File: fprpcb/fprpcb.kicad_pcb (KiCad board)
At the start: 2 copper layers, 119.8 x 90.3 mm, 46 parts, among them J1 Conn_02x04_Odd_Even, J2 Conn_01x02, J3 Conn_01x03, J4 Conn_01x03, J5 Conn_01x03, J6 Conn_01x03, J7 Conn_01x06, J8 Conn_01x04, SW1 Conn_01x02_Pin, SW2 Conn_01x02_Pin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

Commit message: verifying all traces to be correct size and clearance
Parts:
- moved R4 1.10 mm to (119.1, 72.5)
- moved R10 1.10 mm to (155.9, 72.5)
- moved R6 1.10 mm to (143.6, 72.5)
- moved R8 1.10 mm to (131.3, 72.5)
- moved R13 0.97 mm to (168.6, 72.5)
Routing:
- net Net-(SW3-Pin_2): track 6.40 -> 15.2 mm
- net GND: track 502.1 -> 494.1 mm, vias 3 -> 4
- net Net-(SW4-Pin_2): track 6.60 -> 13.3 mm
- net Net-(SW2-Pin_2): track 6.60 -> 13.0 mm
- net /SW3: track 159.2 -> 164.6 mm
- net +3V3: track 55.2 -> 57.7 mm
- net /SW1: track 100.1 -> 101.4 mm
- net Net-(SW1-Pin_2): track 6.79 -> 5.60 mm
- net VDDA: track 117.8 -> 118.9 mm
- net Net-(SW5-Pin_2): track 6.23 -> 5.27 mm

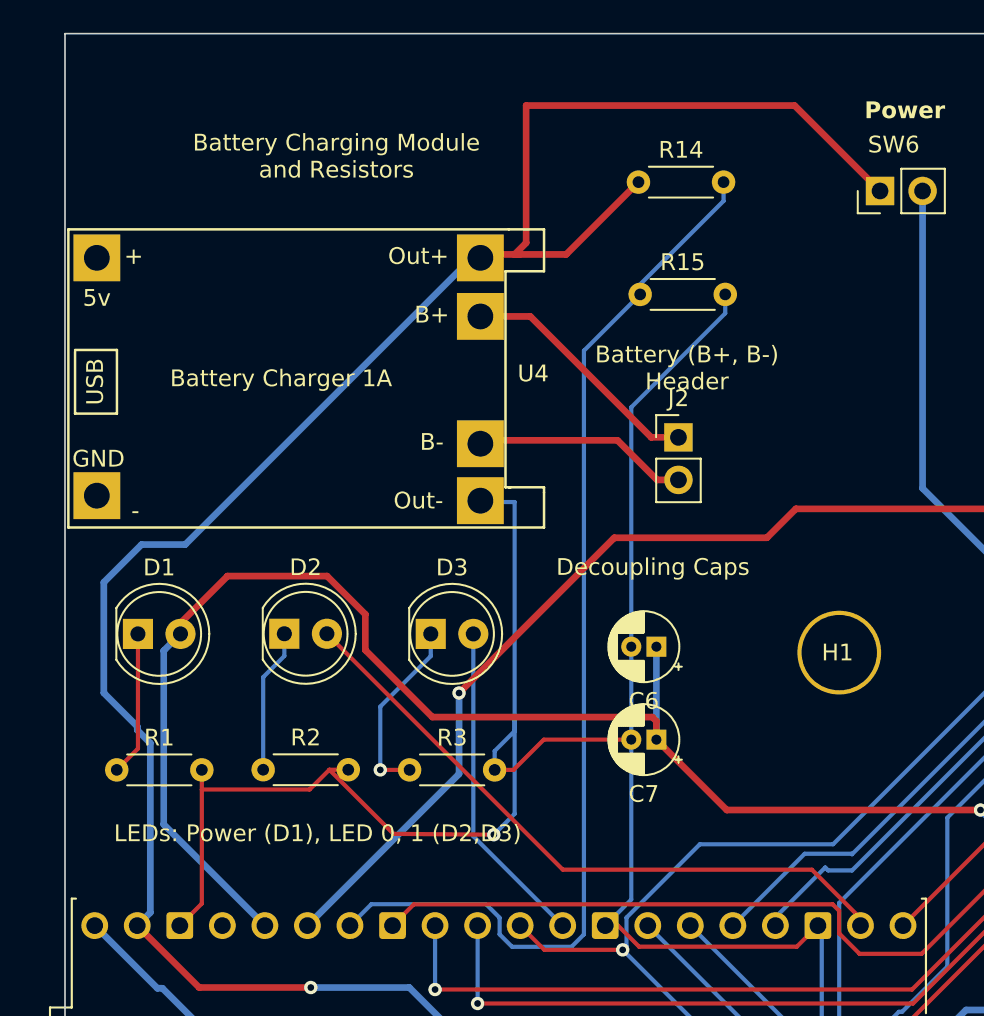
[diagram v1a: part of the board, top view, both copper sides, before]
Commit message: Updated FPRPCB based on 3/30 feedback
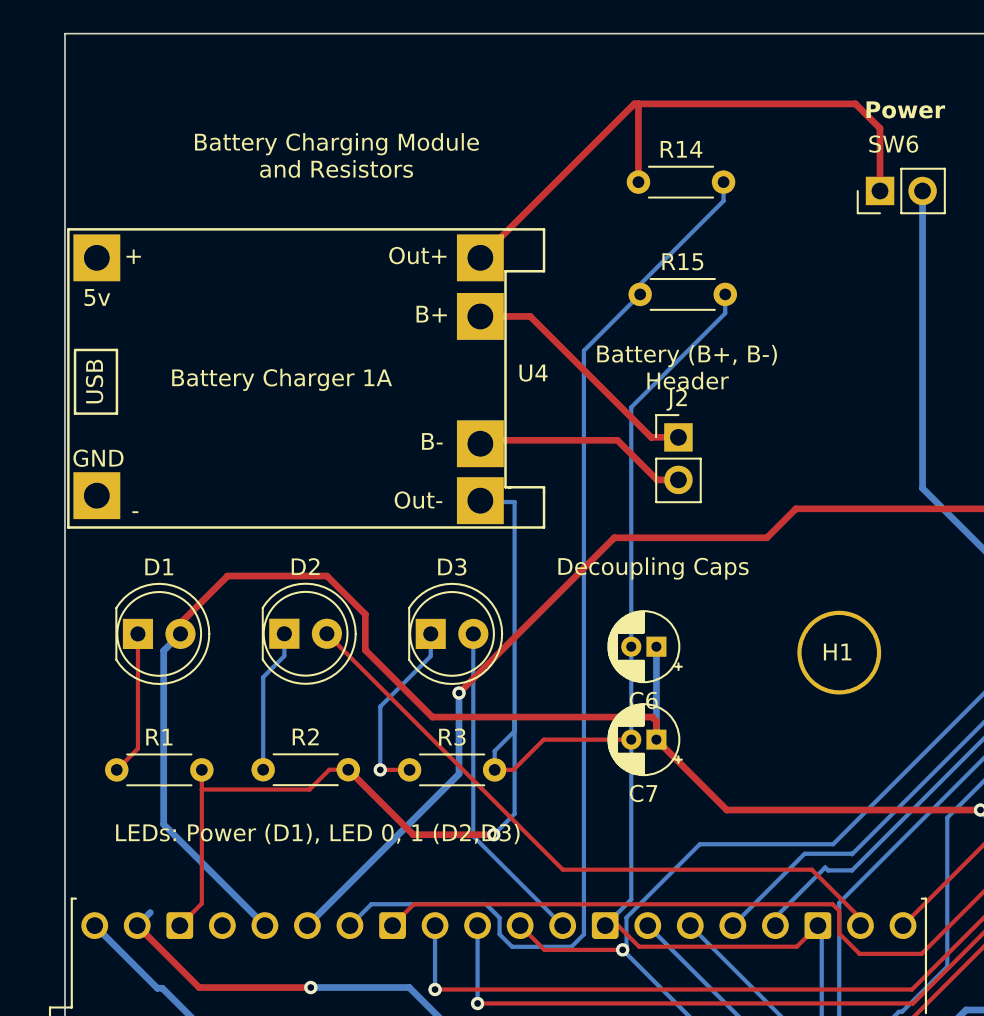
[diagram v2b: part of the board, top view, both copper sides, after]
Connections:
- R14 pad 1: VSYS -> Out+
- SW6 pad 1: VSYS -> Out+
- U4 pad 1: VSYS -> Out+
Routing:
- net VSYS: track 317.7 -> 222.4 mm
- net Out+: track 0.00 -> 36.7 mm
- net GND: track 494.1 -> 493.0 mm
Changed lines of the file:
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@@
   (net 49 "/B-")
   (net 50 "VSYS")
+  (net 51 "Out+")
   (footprint "LED_THT:LED_D5.0mm" (layer "F.Cu")
     (at 64.299 95.1484)
@@
       (stroke (width 0.15) (type solid)) (layer "F.SilkS"))
     (pad "1" thru_hole rect (at 24.6 1.7) (size 2.8 2.8) (drill 1.54) (layers "*.Cu" "*.Mask")
-      (net 50 "VSYS") (pinfunction "OUT+") (pintype "power_in"))
+      (net 51 "Out+") (pinfunction "OUT+") (pintype "power_in"))
     (pad "2" thru_hole rect (at 24.6 5.2) (size 2.8 2.8) (drill 1.54) (layers "*.Cu" "*.Mask")
       (net 48 "/B+") (pinfunction "B+") (pintype "power_in"))
@@
       (stroke (width 0.1) (type solid)) (layer "F.Fab"))
     (pad "1" thru_hole circle (at 0 0) (size 1.4 1.4) (drill 0.7) (layers "*.Cu" "*.Mask")
-      (net 50 "VSYS") (pintype "passive"))
+      (net 51 "Out+") (pintype "passive"))
     (pad "2" thru_hole oval (at 5.08 0) (size 1.4 1.4) (drill 0.7) (layers "*.Cu" "*.Mask")
       (net 45 "/GP28_ADC2") (pintype "passive"))
@@
       (stroke (width 0.1) (type solid)) (layer "F.Fab"))
     (pad "1" thru_hole rect (at 0 0 90) (size 1.7 1.7) (drill 1) (layers "*.Cu" "*.Mask")
-      (net 50 "VSYS") (pinfunction "Pin_1") (pintype "passive"))
+      (net 51 "Out+") (pinfunction "Pin_1") (pintype "passive"))
     (pad "2" thru_hole oval (at 0 2.54 90) (size 1.7 1.7) (drill 1) (layers "*.Cu" "*.Mask")
       (net 50 "VSYS") (pinfunction "Pin_2") (pintype "passive"))
@@
   (segment (start 148.0092 82.4039) (end 158.556 82.4039) (width 0.25) (layer "F.Cu") (net 2))
   (segment (start 68.114 104.439) (end 68.114 103.2674) (width 0.25) (layer "F.Cu") (net 2))
-  (segment (start 75.7291 103.2584) (end 79.5571 107.0864) (width 0.25) (layer "F.Cu") (net 2))
   (segment (start 89.154 138.7856) (end 76.2508 138.7856) (width 0.25) (layer "F.Cu") (net 2))
+  (segment (start 76.856 103.2584) (end 80.7348 107.1372) (width 0.4) (layer "F.Cu") (net 2))
   (segment (start 148.0092 82.4039) (end 146.9129 83.5002) (width 0.25) (layer "F.Cu") (net 2))
   (segment (start 103.6707 131.5712) (end 104.898 130.3439) (width 0.25) (layer "F.Cu") (net 2))
+  (segment (start 80.7348 107.1372) (end 85.5472 107.1372) (width 0.4) (layer "F.Cu") (net 2))
   (segment (start 88.5319 101.4604) (end 86.7249 103.2674) (width 0.25) (layer "F.Cu") (net 2))
   (segment (start 66.798 130.3439) (end 67.0649 130.3439) (width 0.25) (layer "F.Cu") (net 2))
@@
   (segment (start 68.114 111.2479) (end 68.114 104.439) (width 0.25) (layer "F.Cu") (net 2))
   (segment (start 124.51 85.4456) (end 135.5811 85.4456) (width 0.25) (layer "F.Cu") (net 2))
-  (segment (start 79.5571 107.0864) (end 85.5472 107.1372) (width 0.25) (layer "F.Cu") (net 2))
   (segment (start 146.9129 83.828) (end 146.2138 84.5271) (width 0.25) (layer "F.Cu") (net 2))
   (segment (start 162.3463 71.1708) (end 172.5676 71.1708) (width 0.4) (layer "F.Cu") (net 2))
@@
   (segment (start 65.8368 106.5227) (end 71.878 112.5639) (width 0.4) (layer "B.Cu") (net 6))
   (segment (start 95.2538 101.4604) (end 95.2538 95.9104) (width 0.4) (layer "B.Cu") (net 6))
-  (segment (start 63.034 103.2674) (end 64.299 102.0024) (width 0.25) (layer "F.Cu") (net 7))
   (segment (start 64.299 102.0024) (end 64.299 95.1484) (width 0.25) (layer "F.Cu") (net 7))
+  (segment (start 64.299 102.0024) (end 63.034 103.2674) (width 0.25) (layer "F.Cu") (net 7))
   (segment (start 71.776 97.7313) (end 73.041 96.4663) (width 0.25) (layer "B.Cu") (net 8))
   (segment (start 73.041 95.1394) (end 73.041 96.4663) (width 0.25) (layer "B.Cu") (net 8))
@@
   (segment (start 95.2939 85.9536) (end 92.9314 83.5911) (width 0.4) (layer "F.Cu") (net 49))
   (segment (start 92.9314 83.5911) (end 84.7749 83.5911) (width 0.4) (layer "F.Cu") (net 49))
-  (segment (start 87.4776 71.8026) (end 86.7891 72.4911) (width 0.4) (layer "F.Cu") (net 50))
   (segment (start 120.0404 95.3516) (end 120.0404 101.0412) (width 0.4) (layer "F.Cu") (net 50))
-  (segment (start 84.7749 72.4911) (end 84.5712 72.6948) (width 0.4) (layer "F.Cu") (net 50))
-  (segment (start 87.0712 72.4911) (end 84.7749 72.4911) (width 0.4) (layer "F.Cu") (net 50))
   (segment (start 96.4692 125.4252) (end 98.298 127.254) (width 0.4) (layer "F.Cu") (net 50))
   (segment (start 78.8416 143.8148) (end 82.042 147.0152) (width 0.4) (layer "F.Cu") (net 50))
-  (segment (start 87.4776 63.6016) (end 87.4776 71.8026) (width 0.4) (layer "F.Cu") (net 50))
-  (segment (start 103.504 63.6016) (end 87.4776 63.6016) (width 0.4) (layer "F.Cu") (net 50))
   (segment (start 118.0592 143.5608) (end 118.0592 142.2908) (width 0.4) (layer "F.Cu") (net 50))
   (segment (start 82.042 147.0152) (end 114.6048 147.0152) (width 0.4) (layer "F.Cu") (net 50))
   (segment (start 67.9551 116.261) (end 74.6204 116.261) (width 0.4) (layer "F.Cu") (net 50))
-  (segment (start 89.8657 72.4911) (end 94.1832 68.1736) (width 0.4) (layer "F.Cu") (net 50))
   (segment (start 117.856 127.254) (end 117.9068 127.2032) (width 0.4) (layer "F.Cu") (net 50))
   (segment (start 116.2304 145.3896) (end 118.0592 143.5608) (width 0.4) (layer "F.Cu") (net 50))
@@
   (segment (start 116.2304 91.5416) (end 120.0404 95.3516) (width 0.4) (layer "F.Cu") (net 50))
   (segment (start 116.2304 145.5928) (end 116.2304 145.3896) (width 0.4) (layer "F.Cu") (net 50))
-  (segment (start 108.6054 68.703) (end 103.504 63.6016) (width 0.4) (layer "F.Cu") (net 50))
-  (segment (start 86.7891 72.4911) (end 87.0712 72.4911) (width 0.4) (layer "F.Cu") (net 50))
   (segment (start 98.298 127.254) (end 117.856 127.254) (width 0.4) (layer "F.Cu") (net 50))
-  (segment (start 87.0712 72.4911) (end 89.8657 72.4911) (width 0.4) (layer "F.Cu") (net 50))
   (segment (start 64.258 112.5639) (end 67.9551 116.261) (width 0.4) (layer "F.Cu") (net 50))
   (segment (start 114.6048 147.0152) (end 116.0272 145.5928) (width 0.4) (layer "F.Cu") (net 50))
@@
   (via (at 116.2304 145.5928) (size 0.8) (drill 0.4) (layers "F.Cu" "B.Cu") (net 50))
   (segment (start 120.0404 101.0412) (end 121.9708 101.0412) (width 0.4) (layer "B.Cu") (net 50))
-  (segment (start 67.1197 89.8144) (end 64.516 89.8144) (width 0.4) (layer "B.Cu") (net 50))
   (segment (start 127 144.0688) (end 127 114.5032) (width 0.4) (layer "B.Cu") (net 50))
   (segment (start 111.1454 68.703) (end 111.1454 86.4566) (width 0.4) (layer "B.Cu") (net 50))
   (segment (start 125.476 145.5928) (end 127 144.0688) (width 0.4) (layer "B.Cu") (net 50))
-  (segment (start 65.0368 101.6676) (end 65.0368 111.7851) (width 0.4) (layer "B.Cu") (net 50))
   (segment (start 80.4994 116.261) (end 74.6204 116.261) (width 0.4) (layer "B.Cu") (net 50))
   (segment (start 127 114.5032) (end 131.3942 110.109) (width 0.4) (layer "B.Cu") (net 50))
@@
   (segment (start 122.3264 101.0412) (end 122.2248 101.0412) (width 0.4) (layer "B.Cu") (net 50))
   (segment (start 118.0592 127.3556) (end 118.0592 142.2908) (width 0.4) (layer "B.Cu") (net 50))
-  (segment (start 64.258 100.6673) (end 64.258 100.8888) (width 0.4) (layer "B.Cu") (net 50))
   (segment (start 122.2248 101.0412) (end 120.0404 101.0412) (width 0.4) (layer "B.Cu") (net 50))
   (segment (start 89.6636 125.4252) (end 80.4994 116.261) (width 0.4) (layer "B.Cu") (net 50))
   (segment (start 122.2248 101.0412) (end 121.9708 101.0412) (width 0.4) (layer "B.Cu") (net 50))
-  (segment (start 84.443 72.4911) (end 67.1197 89.8144) (width 0.4) (layer "B.Cu") (net 50))
   (segment (start 131.3942 110.109) (end 122.3264 101.0412) (width 0.4) (layer "B.Cu") (net 50))
   (segment (start 96.4692 125.4252) (end 89.6636 125.4252) (width 0.4) (layer "B.Cu") (net 50))
-  (segment (start 62.26255 92.06785) (end 62.26255 98.67185) (width 0.4) (layer "B.Cu") (net 50))
   (segment (start 65.0368 111.7851) (end 64.258 112.5639) (width 0.4) (layer "B.Cu") (net 50))
   (segment (start 78.8416 143.8148) (end 78.8416 141.2748) (width 0.4) (layer "B.Cu") (net 50))
   (segment (start 111.1454 86.4566) (end 116.2304 91.5416) (width 0.4) (layer "B.Cu") (net 50))
-  (segment (start 62.26255 98.67185) (end 64.258 100.6673) (width 0.4) (layer "B.Cu") (net 50))
-  (segment (start 64.516 89.8144) (end 62.26255 92.06785) (width 0.4) (layer "B.Cu") (net 50))
-  (segment (start 64.258 100.8888) (end 65.0368 101.6676) (width 0.4) (layer "B.Cu") (net 50))
   (segment (start 116.2304 145.5928) (end 125.476 145.5928) (width 0.4) (layer "B.Cu") (net 50))
+  (segment (start 94.1832 63.5) (end 107.1372 63.5) (width 0.4) (layer "F.Cu") (net 51))
+  (segment (start 84.744 72.6948) (end 93.9388 63.5) (width 0.4) (layer "F.Cu") (net 51))
+  (segment (start 107.1372 63.5) (end 108.6054 64.9682) (width 0.4) (layer "F.Cu") (net 51))
+  (segment (start 94.1832 63.5) (end 94.1832 68.1736) (width 0.4) (layer "F.Cu") (net 51))
+  (segment (start 108.6054 64.9682) (end 108.6054 68.703) (width 0.4) (layer "F.Cu") (net 51))
+  (segment (start 93.9388 63.5) (end 94.1832 63.5) (width 0.4) (layer "F.Cu") (net 51))
   (zone (net 0) (net_name "") (layer "F.CrtYd") (hatch edge 0.5)
     (connect_pads (clearance 0))
